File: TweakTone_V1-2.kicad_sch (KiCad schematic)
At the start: 55 parts, among them IC1 PT2399, IC2 TL072, M1 PAD8, M2 PAD8

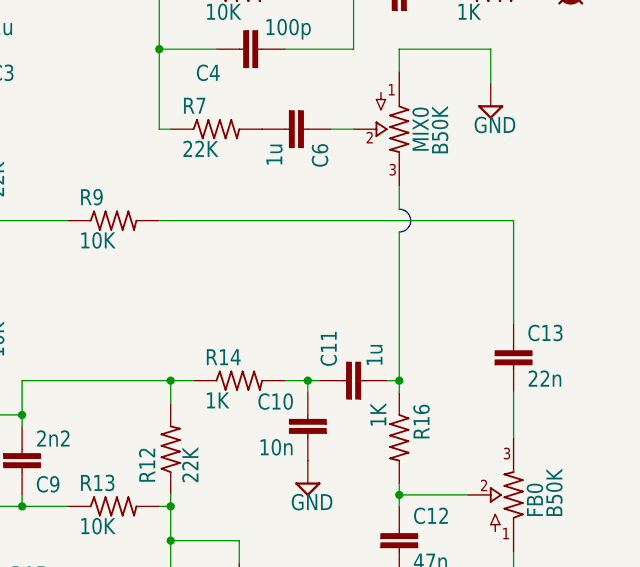
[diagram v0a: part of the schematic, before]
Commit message: fix missing connection between MIX0 and wet signal
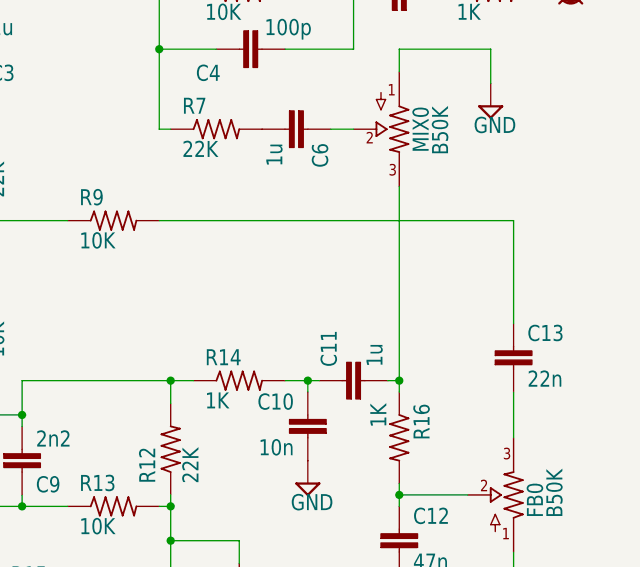
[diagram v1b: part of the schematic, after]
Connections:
- net at MIX0.3: now also C11.2, R16.1
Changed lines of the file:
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@@
 	(generator_version "9.0")
 	(paper "A4")
-	(arc
-		(start 194.31 106.68)
-		(mid 195.58 107.95)
-		(end 194.31 109.22)
-		(stroke
-			(width 0.1524)
-			(type solid)
-		)
-		(fill
-			(type none)
-		)
-	)
 	(junction
 		(at 83.82 41.91)
@@
 	(wire
 		(pts
+			(xy 186.69 97.79) (xy 189.23 97.79)
+		)
+		(stroke
+			(width 0)
+			(type default)
+		)
+	)
+	(wire
+		(pts
 			(xy 118.11 85.09) (xy 118.11 77.47)
 		)
@@
 	(wire
 		(pts
-			(xy 186.69 97.79) (xy 189.23 97.79)
-		)
-		(stroke
-			(width 0.1524)
-			(type solid)
-		)
-	)
-	(wire
-		(pts
 			(xy 189.23 72.39) (xy 184.15 72.39)
 		)
@@
 	(wire
 		(pts
-			(xy 194.31 106.68) (xy 194.31 104.14)
-		)
-		(stroke
-			(width 0.1524)
-			(type solid)
-		)
-	)
-	(wire
-		(pts
 			(xy 121.92 85.09) (xy 118.11 85.09)
 		)
@@
 	(wire
 		(pts
-			(xy 194.31 125.73) (xy 194.31 109.22)
-		)
-		(stroke
+			(xy 194.31 104.14) (xy 194.31 125.73)
+		)
+		(stroke
